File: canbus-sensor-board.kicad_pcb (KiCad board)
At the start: 4 copper layers, 32 x 39 mm, 51 parts, among them J1 CAN IO, J10 Conn_01x01, J11 Conn_01x01, J2 CAN Term, J3 POWER IN, J4 Conn_01x01, J5 I2C2 IO, J6 I2C1 IO, J7 Conn_01x01, J8 Conn_ARM_SWD_TagConnect_TC203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, J9 Conn_01x01, Q1 AO3400A, Q2 AO3400A, Q3 AO3400A, Q4 AO3400A, U1 MCP2551-I-SN, U3 AMS1117-3.3, U4 STM32F103C8Tx

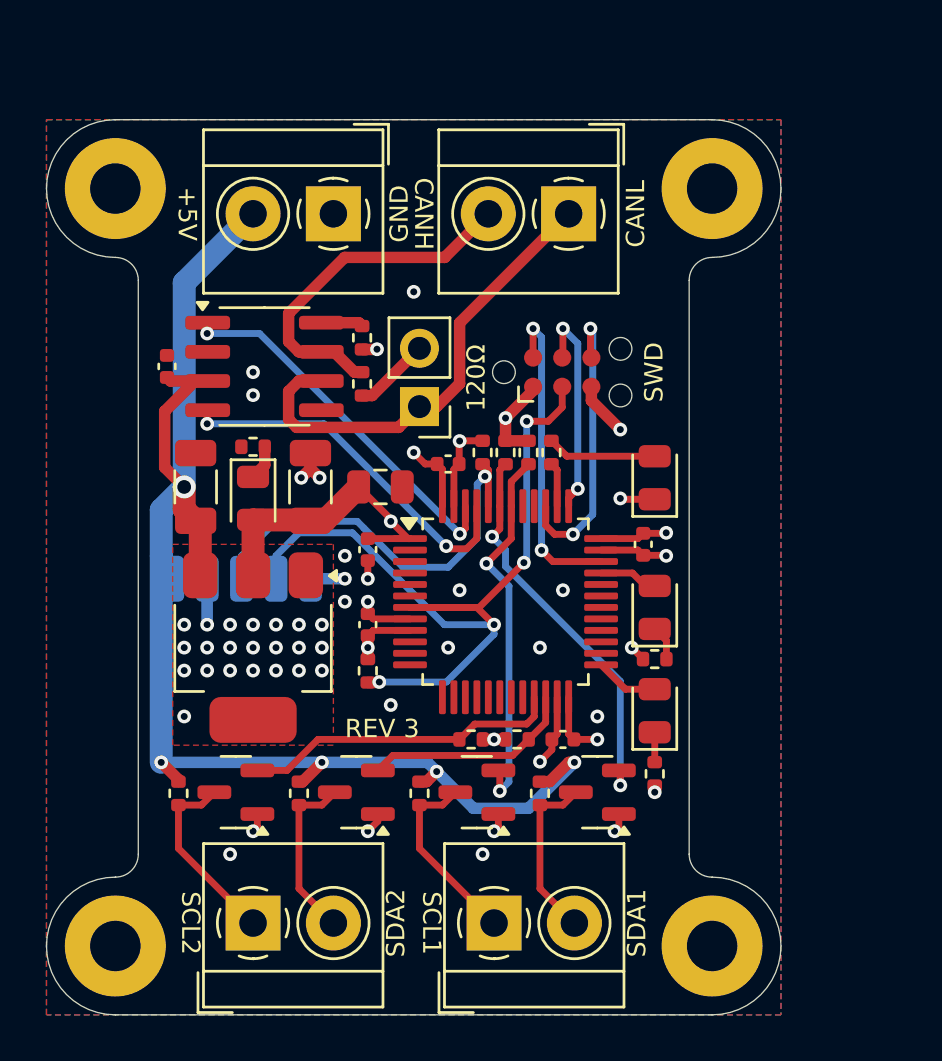
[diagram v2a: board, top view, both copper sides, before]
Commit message: Further tweak rev4 of the board
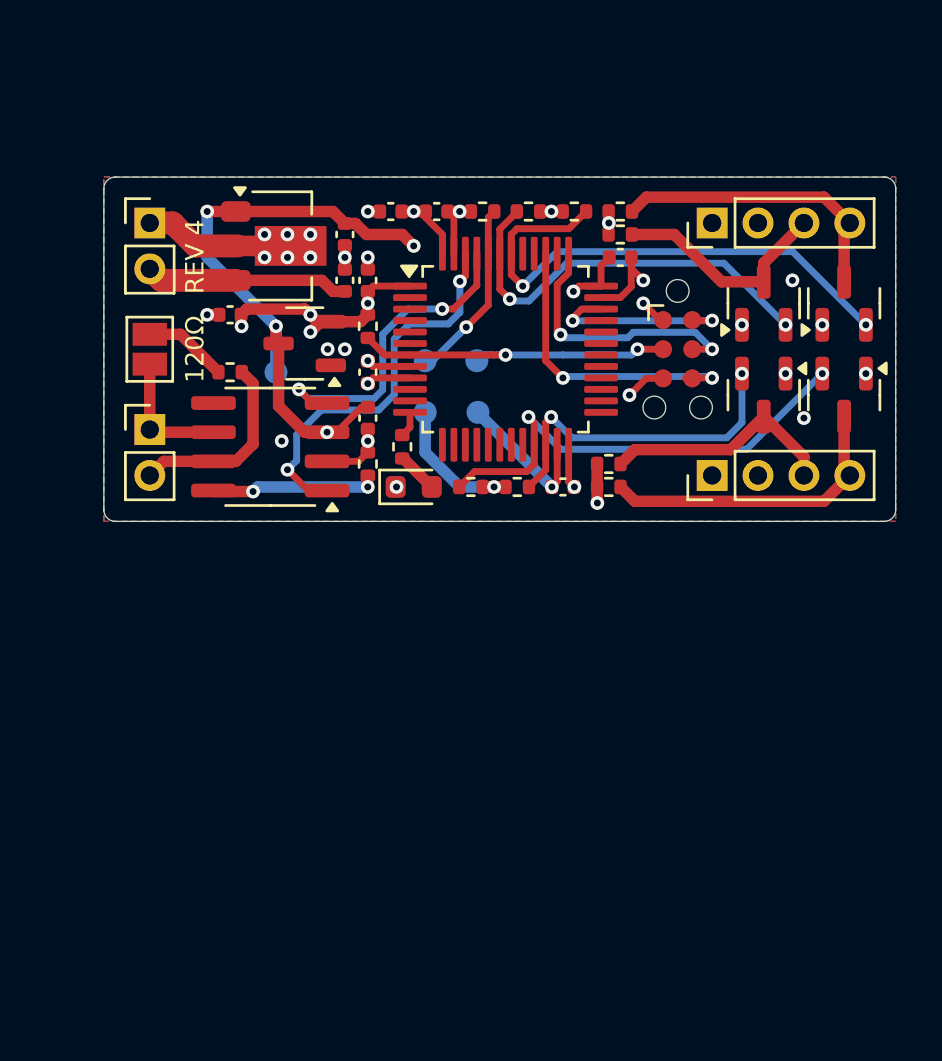
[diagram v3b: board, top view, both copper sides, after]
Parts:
- removed D2: Debug LED 1 RED, LED_SMD:LED_0805_2012Metric
- removed D3: Debug LED 3 GREEN, LED_SMD:LED_0805_2012Metric
- removed D5: Debug LED 2 YELLOW, LED_SMD:LED_0805_2012Metric
- removed H1, H2, H3, H4: MountingHole_Pad, MountingHole:MountingHole_2.2mm_M2_Pad
- removed R14, R15, R16: 10k, Resistor_SMD:R_0402_1005Metric
- added C10: 100n, Capacitor_SMD:C_0402_1005Metric, F.Cu at (34.0, 37.0)
- added U2: MCP2551-I-SN, Package_SO:SOIC-8_3.9x4.9mm_P1.27mm, F.Cu at (29.8, 44.2)
- C2, C3, C5: value 100n -> 10u
- C4: footprint Capacitor_SMD:C_0805_2012Metric -> Capacitor_SMD:C_0402_1005Metric
- C6, C7: value 22u -> 100n; footprint Capacitor_SMD:C_1206_3216Metric -> Capacitor_SMD:C_0402_1005Metric
- D1: value Power (GREEN) -> STATUS LED RED; footprint LED_SMD:LED_0805_2012Metric -> LED_SMD:LED_0603_1608Metric
- J1: value CAN IO -> Conn_ARM_SWD_TagConnect_TC2030-NL; footprint TerminalBlock_4Ucon:TerminalBlock_4Ucon_1x02_P3.50mm_Horizontal -> Connector:Tag-Connect_TC2030-IDC-NL_2x03_P1.27mm_Vertical
- J10, J11: value Conn_01x01 -> Conn_01x04_Socket; footprint Connector_Wire:SolderWirePad_1x01_SMD_1x2mm -> Connector_PinHeader_2.00mm:PinHeader_1x04_P2.00mm_Vertical; moved to F.Cu
- J2: value CAN Term -> Conn_01x01; footprint Connector_PinHeader_2.54mm:PinHeader_1x02_P2.54mm_Vertical -> TestPoint:TestPoint_Pad_D1.0mm; moved to B.Cu
- J3: value POWER IN -> Conn_01x01; footprint TerminalBlock_4Ucon:TerminalBlock_4Ucon_1x02_P3.50mm_Horizontal -> TestPoint:TestPoint_Pad_D1.0mm; moved to B.Cu
- J4: footprint Connector_Wire:SolderWirePad_1x01_SMD_1x2mm -> TestPoint:TestPoint_Pad_D1.0mm
- J5: value I2C2 IO -> Conn_01x01; footprint TerminalBlock_4Ucon:TerminalBlock_4Ucon_1x02_P3.50mm_Horizontal -> TestPoint:TestPoint_Pad_D1.0mm; moved to B.Cu
- J6: value I2C1 IO -> Conn_01x01; footprint TerminalBlock_4Ucon:TerminalBlock_4Ucon_1x02_P3.50mm_Horizontal -> TestPoint:TestPoint_Pad_D1.0mm; moved to B.Cu
- J7: value Conn_01x01 -> Conn_01x02_Socket; footprint Connector_Wire:SolderWirePad_1x01_SMD_1x2mm -> Connector_PinHeader_2.00mm:PinHeader_1x02_P2.00mm_Vertical; moved to F.Cu
- J8: value Conn_ARM_SWD_TagConnect_TC2030-NL -> Conn_01x02_Socket; footprint Connector:Tag-Connect_TC2030-IDC-NL_2x03_P1.27mm_Vertical -> Connector_PinHeader_2.00mm:PinHeader_1x02_P2.00mm_Vertical
- J9: value Conn_01x01 -> CAN Term; footprint Connector_Wire:SolderWirePad_1x01_SMD_1x2mm -> Jumper:SolderJumper-2_P1.3mm_Open_Pad1.0x1.5mm; moved to F.Cu
- R1: value 120 -> 10k
- R10, R11, R13: value 1k -> 10k
- R4: value 10k -> 1k
- R5: value 1k -> 120
- U1: value MCP2551-I-SN -> L78L05_SOT89; footprint Package_SO:SOIC-8_3.9x4.9mm_P1.27mm -> Package_TO_SOT_SMD:SOT-89-3
- U3: value AMS1117-3.3 -> XC6206PxxxMR; footprint Package_TO_SOT_SMD:SOT-223-3_TabPin2 -> Package_TO_SOT_SMD:SOT-23-3
- moved Q3 31.6 mm to (54.8, 42.0), turned to -90 degrees
- moved Q1 26.6 mm to (54.8, 38.0), turned to 90 degrees
- moved R12 25.9 mm to (45.0, 35.0), turned to 180 degrees
- moved J6 25.8 mm to (30.0, 41.0), turned to 180 degrees
- moved Q4 24.8 mm to (51.2, 42.0), turned to -90 degrees
- moved J5 23.5 mm to (36.5, 42.8), turned to 180 degrees
- moved J10 23.4 mm to (49.0, 34.5), turned to 90 degrees
- moved R8 23.1 mm to (41.0, 34.0)
- moved Q2 22.5 mm to (51.2, 38.0), turned to 90 degrees
- moved J11 22.5 mm to (49.0, 45.5), turned to 90 degrees
- moved C2 22.1 mm to (33.0, 37.0), turned to 90 degrees
- moved R3 20.6 mm to (39.0, 34.0), turned to 0 degrees
- moved C3 18.7 mm to (33.0, 35.0)
- moved J8 18.1 mm to (24.5, 43.5)
- moved C7 16.8 mm to (45.0, 36.0), turned to 0 degrees
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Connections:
- C1 pad 1: +3.3V -> +5V
- C2 pad 1: +3.3V -> +12V
- C3 pad 1: +3.3V -> +5V
- C5 pad 1: +5V -> +3.3V
- C6 pad 1: +5V -> +3.3V
- D1 pad 1: Net-(D1-K) -> GND
- D1 pad 2: +3.3V -> Net-(D1-A)
- J1 pad 1: CANL -> +3.3V
- J1 pad 2: CANH -> SWDIO
- J11 pad 1: +3.3V -> GND
- J2 pad 1: CANL -> BOOT
- J3 pad 1: GND -> NRST
- J4 pad 1: +5V -> GND
- J5 pad 1: I2C2_SCL_5V -> +3.3V
- J6 pad 1: I2C1_SCL_5V -> +5V
- J7 pad 1: BOOT -> GND
- J8 pad 1: +3.3V -> CANL
- J8 pad 2: SWDIO -> CANH
- J9 pad 1: NRST -> CANL
- R1 pad 1: CANH -> GND
- R1 pad 2: Net-(J2-Pin_2) -> Net-(U2-Rs)
- R10 pad 1: DEBUG_LED1 -> I2C1_SCL_5V
- R10 pad 2: Net-(D2-A) -> +5V
- R11 pad 1: Net-(D3-K) -> I2C2_SCL_5V
- R11 pad 2: GND -> +5V
- R12 pad 1: I2C1_SCL_5V -> I2C1_SDA_5V
- R13 pad 1: Net-(D5-K) -> I2C2_SDA_5V
- R13 pad 2: GND -> +5V
- R2 pad 1: GND -> NRST
- R2 pad 2: Net-(U1-Rs) -> +3.3V
- R3 pad 1: NRST -> GND
- R3 pad 2: +3.3V -> BOOT
- R4 pad 1: GND -> STATUS_LED
- R4 pad 2: BOOT -> Net-(D1-A)
- R5 pad 1: GND -> CANH
- R5 pad 2: Net-(D1-K) -> Net-(J9-Pin_2)
- R7 pad 1: I2C1_SDA -> I2C2_SCL
- R8 pad 1: I2C2_SCL -> I2C1_SDA
- U1 pad 1: CAN_TX -> +5V
- U1 pad 3: +5V -> +12V
- U4 pad 12: unconnected-(U4-PA2-Pad12) -> STATUS_LED
- U4 pad 25: DEBUG_LED3 -> unconnected-(U4-PB12-Pad25)
- U4 pad 33: DEBUG_LED2 -> unconnected-(U4-PA12-Pad33)
- U4 pad 38: DEBUG_LED1 -> unconnected-(U4-PA15-Pad38)
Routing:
- net NRST: track 38.0 -> 14.6 mm, vias 4 -> 2
- net CANL: track 20.6 -> 5.67 mm
- net BOOT: track 18.2 -> 7.94 mm
- net +12V: track 0.00 -> 8.91 mm
- net Net-(U2-Rs): track 0.00 -> 7.32 mm, vias 0 -> 2
- net CANH: track 15.5 -> 8.40 mm
- net I2C2_SCL: track 13.9 -> 20.6 mm, vias 0 -> 2
- net I2C1_SCL: track 16.5 -> 23.0 mm
- net +3.3V: track 35.0 -> 28.9 mm, vias 32 -> 15
- net SWDIO: track 13.9 -> 8.47 mm
- net +5V: track 62.5 -> 67.9 mm, vias 5 -> 6
- net I2C2_SDA: track 9.28 -> 14.6 mm, vias 0 -> 2
- net I2C2_SCL_5V: track 8.28 -> 13.4 mm
- net GND: track 22.1 -> 27.0 mm, vias 27 -> 22
- net Net-(D2-A): track 4.78 -> 0.00 mm
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- added copper zone on In2.Cu, net +3.3V
- added copper zone on In1.Cu, net GND
- removed copper zone on F.Cu, net +3.3V
- removed copper zone on In1.Cu, net +3.3V
- removed copper zone on In2.Cu, net GND
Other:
- board size 32 x 39 mm -> 34.5 x 15 mm
- board text added: "+12/24V"
- board text added: "+3.3V"
- board text added: "CANBUS SENSOR BOARD REV 4 ©2024 dflemstr"
- board text added: "REV 4"
- board text added: "⏚"
- board text removed: "3.3V"
- board text removed: "5V"
- board text removed: "CANBUS SENSOR BOARD REV 3 © 2024 David Flemström"
- board text removed: "REV 3"
- board text removed: "SWD"

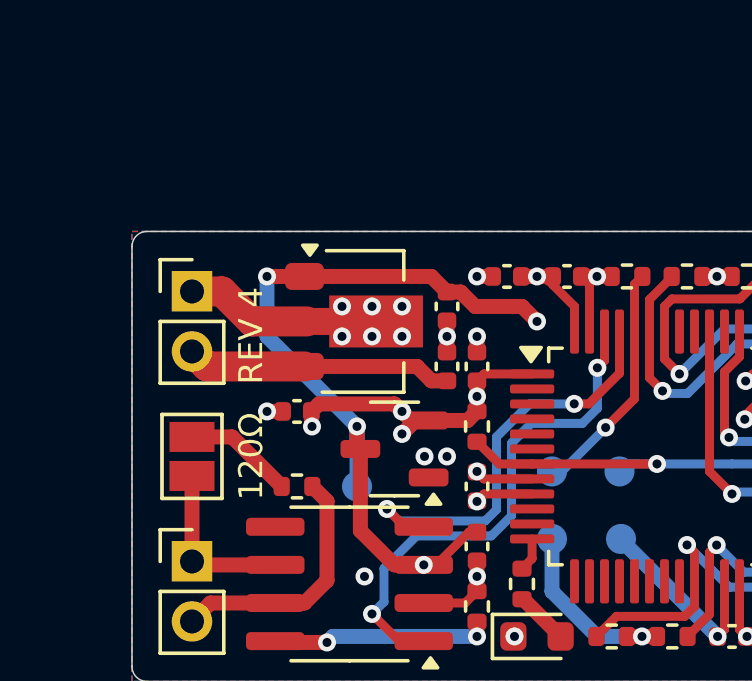
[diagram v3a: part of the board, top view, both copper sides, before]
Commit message: Increase 12-24V cap size so it actually handles that voltage range
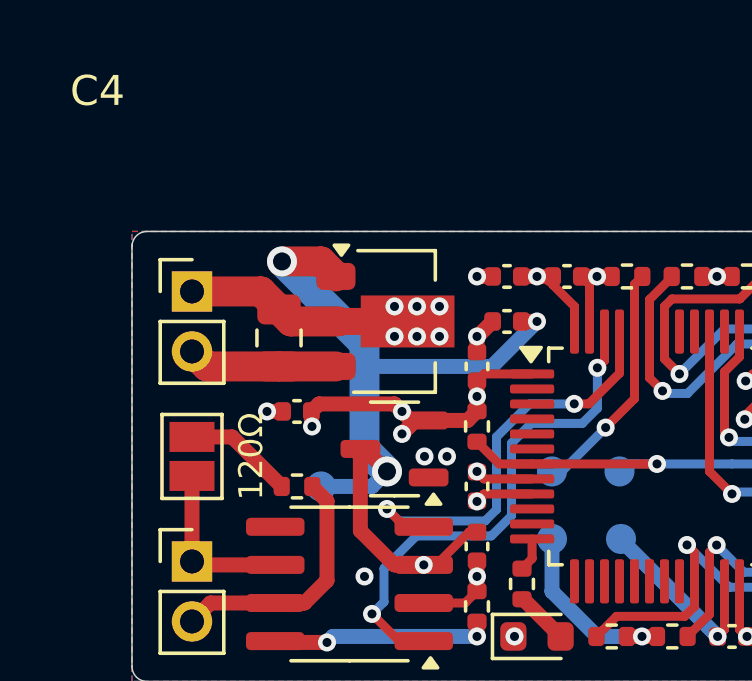
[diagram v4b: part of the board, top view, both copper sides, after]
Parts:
- removed the C2 at (33.0, 37.0)
- added C1: 10u >24V, Capacitor_SMD:C_0805_2012Metric, F.Cu at (27.4, 36.0)
- moved C2 2.06 mm to (35.0, 35.5), turned to 180 degrees
- moved J7 1.20 mm to (28.8, 41.0)
- moved U1 1.05 mm to (31.2, 35.5)
- renumbered C1 to C10, C3 to C2, C4 to C3, C5 to C4, C6 to C5, C7 to C6, C8 to C7, C9 to C8, C10 to C9, J9 to J2, J2 to J3, J3 to J4, J4 to J5, J5 to J6, J6 to J7, J7 to J8, J8 to J9, Q3 to Q2, Q2 to Q3, R4 to R1, R5 to R2, R2 to R3, R3 to R4, R1 to R5, U3 to U2, U4 to U3, U2 to U4
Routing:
- net +12V: track 8.91 -> 5.01 mm
- net +5V: track 67.9 -> 70.1 mm
- net GND: track 27.0 -> 27.8 mm, vias 22 -> 21
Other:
- board text added: "CANBUS SENSOR BOARD REV 5 ©2024 dflemstr"
- board text removed: "CANBUS SENSOR BOARD REV 4 ©2024 dflemstr"
- board text removed: "GND"
- board text removed: "REV 4"
